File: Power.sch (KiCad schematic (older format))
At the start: 0 parts

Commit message: Added Powercontrol stuff
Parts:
- added C? (x2): C, ~, symbol C
- added F? (x4): FUSE, ~, symbol FUSE
- added L? (x2): INDUCTOR, ~, symbol INDUCTOR
- added P?: CONN_12X2, symbol CONN_12X2
- added R?: R, ~, symbol R
- added SW?: SWITCH_INV, ~, symbol SWITCH_INV
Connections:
- net labels added: +12P, +12V, +3,3V, +5V, -12P, -12V, GND
- wire segments 0 -> 39

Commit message: Fan/Current Module Refactoring
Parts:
- removed F? (x4): FUSE, ~, symbol FUSE
- added TH? (x4): THERMISTOR, ~, symbol THERMISTOR
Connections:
- net labels added: +12C
- wire segments 39 -> 40
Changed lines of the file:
@@
 $Descr A4 11693 8268
 encoding utf-8
-Sheet 5 9
+Sheet 4 9
 Title ""
-Date "6 feb 2014"
+Date "7 feb 2014"
 Rev ""
 Comp ""
@@
 $EndComp
 $Comp
-L FUSE F?
-U 1 1 52F10550
-P 3400 1950
-F 0 "F?" H 3500 2000 40  0000 C CNN
-F 1 "FUSE" H 3300 1900 40  0000 C CNN
-F 2 "~" H 3400 1950 60  0000 C CNN
-F 3 "~" H 3400 1950 60  0000 C CNN
-	1    3400 1950
-	1    0    0    -1
-$EndComp
-$Comp
-L FUSE F?
-U 1 1 52F1055D
-P 3950 2150
-F 0 "F?" H 4050 2200 40  0000 C CNN
-F 1 "FUSE" H 3850 2100 40  0000 C CNN
-F 2 "~" H 3950 2150 60  0000 C CNN
-F 3 "~" H 3950 2150 60  0000 C CNN
-	1    3950 2150
-	1    0    0    -1
-$EndComp
-$Comp
-L FUSE F?
-U 1 1 52F10563
-P 4500 2350
-F 0 "F?" H 4600 2400 40  0000 C CNN
-F 1 "FUSE" H 4400 2300 40  0000 C CNN
-F 2 "~" H 4500 2350 60  0000 C CNN
-F 3 "~" H 4500 2350 60  0000 C CNN
-	1    4500 2350
-	1    0    0    -1
-$EndComp
-$Comp
-L FUSE F?
-U 1 1 52F10569
-P 5050 2550
-F 0 "F?" H 5150 2600 40  0000 C CNN
-F 1 "FUSE" H 4950 2500 40  0000 C CNN
-F 2 "~" H 5050 2550 60  0000 C CNN
-F 3 "~" H 5050 2550 60  0000 C CNN
-	1    5050 2550
-	1    0    0    -1
-$EndComp
-$Comp
 L SWITCH_INV SW?
 U 1 1 52F105A3
@@
 	5400 2550 5300 2550
 Wire Wire Line
-	4300 1500 4300 2150
-Wire Wire Line
-	4300 2150 4200 2150
-Wire Wire Line
-	3750 1500 3750 1950
-Wire Wire Line
-	3750 1950 3650 1950
+	4300 2150 4300 1500
+Wire Wire Line
+	4150 2150 4300 2150
+Wire Wire Line
+	3750 1950 3750 1500
+Wire Wire Line
+	3600 1950 3750 1950
 $Comp
 L INDUCTOR L?
@@
 	8650 2750 8650 2500
 Connection ~ 7800 2750
+$Comp
+L +12C #PWR?
+U 1 1 52F3B02A
+P 3050 1500
+F 0 "#PWR?" H 3050 1470 30  0001 C CNN
+F 1 "+12C" H 3050 1610 40  0000 C CNN
+F 2 "" H 3050 1500 60  0000 C CNN
+F 3 "" H 3050 1500 60  0000 C CNN
+	1    3050 1500
+	1    0    0    -1
+$EndComp
+Wire Wire Line
+	3050 1500 3050 2350
+Connection ~ 3050 2350
+$Comp
+L THERMISTOR TH?
+U 1 1 52F3B361
+P 3350 1950
+F 0 "TH?" V 3450 2000 50  0000 C CNN
+F 1 "THERMISTOR" V 3250 1950 50  0000 C CNN
+F 2 "~" H 3350 1950 60  0000 C CNN
+F 3 "~" H 3350 1950 60  0000 C CNN
+	1    3350 1950
+	0    -1   -1   0
+$EndComp
+$Comp
+L THERMISTOR TH?
+U 1 1 52F3B37D
+P 3900 2150
+F 0 "TH?" V 4000 2200 50  0000 C CNN
+F 1 "THERMISTOR" V 3800 2150 50  0000 C CNN
+F 2 "~" H 3900 2150 60  0000 C CNN
+F 3 "~" H 3900 2150 60  0000 C CNN
+	1    3900 2150
+	0    -1   -1   0
+$EndComp
+$Comp
+L THERMISTOR TH?
+U 1 1 52F3B383
+P 4500 2350
+F 0 "TH?" V 4600 2400 50  0000 C CNN
+F 1 "THERMISTOR" V 4400 2350 50  0000 C CNN
+F 2 "~" H 4500 2350 60  0000 C CNN
+F 3 "~" H 4500 2350 60  0000 C CNN
+	1    4500 2350
+	0    -1   -1   0
+$EndComp
+$Comp
+L THERMISTOR TH?
+U 1 1 52F3B389
+P 5050 2550
+F 0 "TH?" V 5150 2600 50  0000 C CNN
+F 1 "THERMISTOR" V 4950 2550 50  0000 C CNN
+F 2 "~" H 5050 2550 60  0000 C CNN
+F 3 "~" H 5050 2550 60  0000 C CNN
+	1    5050 2550
+	0    -1   -1   0
+$EndComp
 $EndSCHEMATC

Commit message: Am Ende der 4. Woche
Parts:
- added C?: C, ~, symbol C
- added L?: INDUCTOR, ~, symbol INDUCTOR
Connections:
- net labels added: +3.3VP, +5P
- wire segments 40 -> 46
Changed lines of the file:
@@
 Sheet 4 9
 Title ""
-Date "7 feb 2014"
+Date "14 feb 2014"
 Rev ""
 Comp ""
@@
 $EndComp
 $Comp
-L +3,3V #PWR?
-U 1 1 52F10507
-P 3750 1500
-F 0 "#PWR?" H 3750 1460 30  0001 C CNN
-F 1 "+3,3V" H 3750 1610 30  0000 C CNN
-F 2 "" H 3750 1500 60  0000 C CNN
-F 3 "" H 3750 1500 60  0000 C CNN
-	1    3750 1500
-	1    0    0    -1
-$EndComp
-$Comp
 L SWITCH_INV SW?
 U 1 1 52F105A3
@@
 F 3 "" H 4850 1500 60  0000 C CNN
 	1    4850 1500
-	1    0    0    -1
-$EndComp
-$Comp
-L +5V #PWR?
-U 1 1 52F10C00
-P 4300 1500
-F 0 "#PWR?" H 4300 1590 20  0001 C CNN
-F 1 "+5V" H 4300 1590 30  0000 C CNN
-F 2 "" H 4300 1500 60  0000 C CNN
-F 3 "" H 4300 1500 60  0000 C CNN
-	1    4300 1500
 	1    0    0    -1
 $EndComp
@@
 	0    -1   -1   0
 $EndComp
+$Comp
+L +5P #PWR?
+U 1 1 52FDF0C0
+P 4300 1500
+F 0 "#PWR?" H 4300 1630 20  0001 C CNN
+F 1 "+5P" H 4300 1600 30  0000 C CNN
+F 2 "" H 4300 1500 60  0000 C CNN
+F 3 "" H 4300 1500 60  0000 C CNN
+	1    4300 1500
+	1    0    0    -1
+$EndComp
+$Comp
+L +3.3VP #PWR?
+U 1 1 52FDF0CF
+P 3750 1500
+F 0 "#PWR?" H 3800 1530 20  0001 C CNN
+F 1 "+3.3VP" H 3750 1590 30  0000 C CNN
+F 2 "" H 3750 1500 60  0000 C CNN
+F 3 "" H 3750 1500 60  0000 C CNN
+	1    3750 1500
+	1    0    0    -1
+$EndComp
+$Comp
+L INDUCTOR L?
+U 1 1 52FDF0DC
+P 7000 1200
+F 0 "L?" V 6950 1200 40  0000 C CNN
+F 1 "INDUCTOR" V 7100 1200 40  0000 C CNN
+F 2 "~" H 7000 1200 60  0000 C CNN
+F 3 "~" H 7000 1200 60  0000 C CNN
+	1    7000 1200
+	0    -1   -1   0
+$EndComp
+$Comp
+L C C?
+U 1 1 52FDF0E2
+P 7750 1500
+F 0 "C?" H 7750 1600 40  0000 L CNN
+F 1 "C" H 7756 1415 40  0000 L CNN
+F 2 "~" H 7788 1350 30  0000 C CNN
+F 3 "~" H 7750 1500 60  0000 C CNN
+	1    7750 1500
+	1    0    0    -1
+$EndComp
+Wire Wire Line
+	6350 950  6350 1200
+Wire Wire Line
+	6350 1200 6700 1200
+Wire Wire Line
+	7300 1200 8600 1200
+Wire Wire Line
+	7750 1200 7750 1300
+$Comp
+L GND #PWR?
+U 1 1 52FDF0F9
+P 7750 1900
+F 0 "#PWR?" H 7750 1900 30  0001 C CNN
+F 1 "GND" H 7750 1830 30  0001 C CNN
+F 2 "" H 7750 1900 60  0000 C CNN
+F 3 "" H 7750 1900 60  0000 C CNN
+	1    7750 1900
+	1    0    0    -1
+$EndComp
+Wire Wire Line
+	8600 1200 8600 950
+Connection ~ 7750 1200
+$Comp
+L +5P #PWR?
+U 1 1 52FDF142
+P 6350 950
+F 0 "#PWR?" H 6350 1080 20  0001 C CNN
+F 1 "+5P" H 6350 1050 30  0000 C CNN
+F 2 "" H 6350 950 60  0000 C CNN
+F 3 "" H 6350 950 60  0000 C CNN
+	1    6350 950
+	1    0    0    -1
+$EndComp
+$Comp
+L +5V #PWR?
+U 1 1 52FDF14A
+P 8600 950
+F 0 "#PWR?" H 8600 1040 20  0001 C CNN
+F 1 "+5V" H 8600 1040 30  0000 C CNN
+F 2 "" H 8600 950 60  0000 C CNN
+F 3 "" H 8600 950 60  0000 C CNN
+	1    8600 950
+	1    0    0    -1
+$EndComp
+Wire Wire Line
+	7750 1700 7750 1900
 $EndSCHEMATC

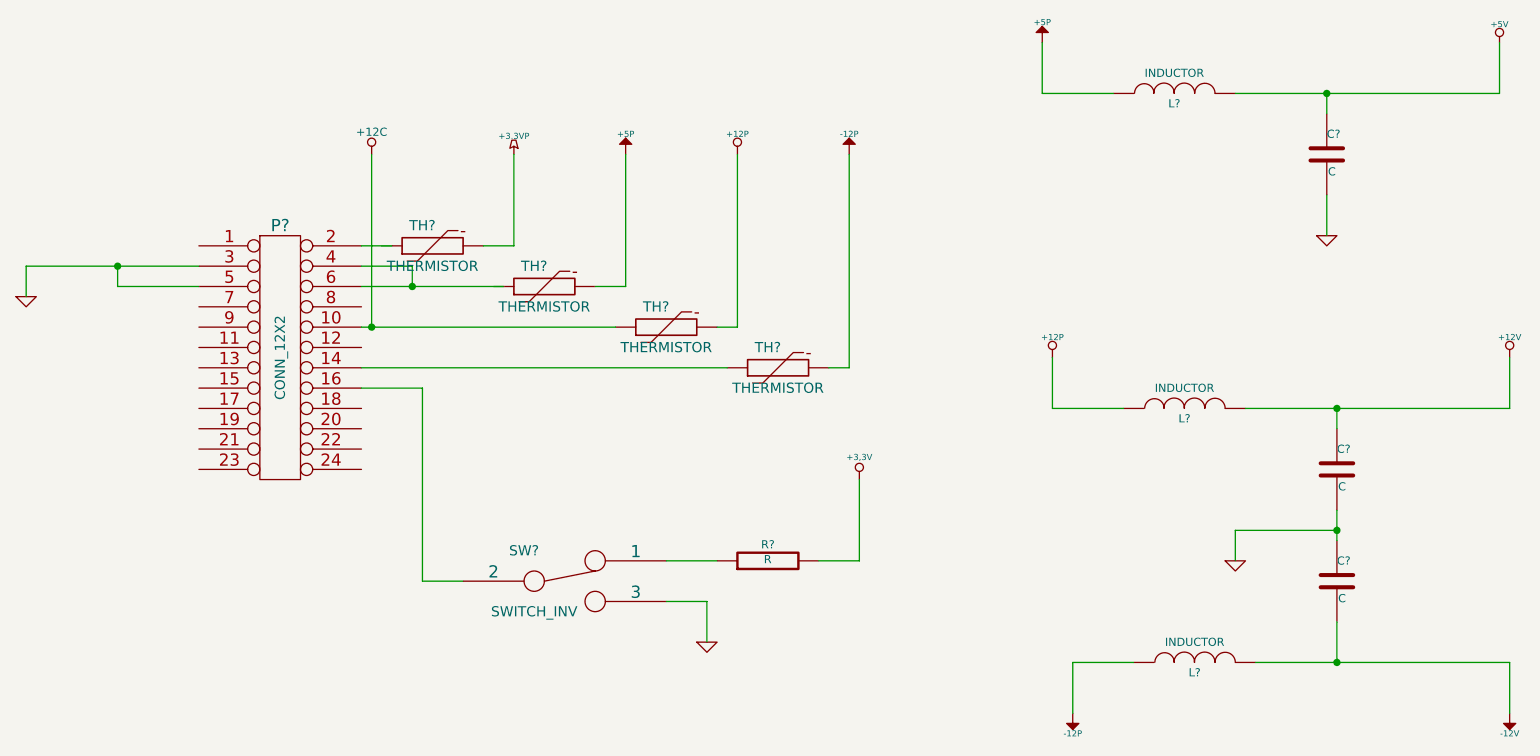
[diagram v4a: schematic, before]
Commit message: Nach Einfuegen Relay-Modul
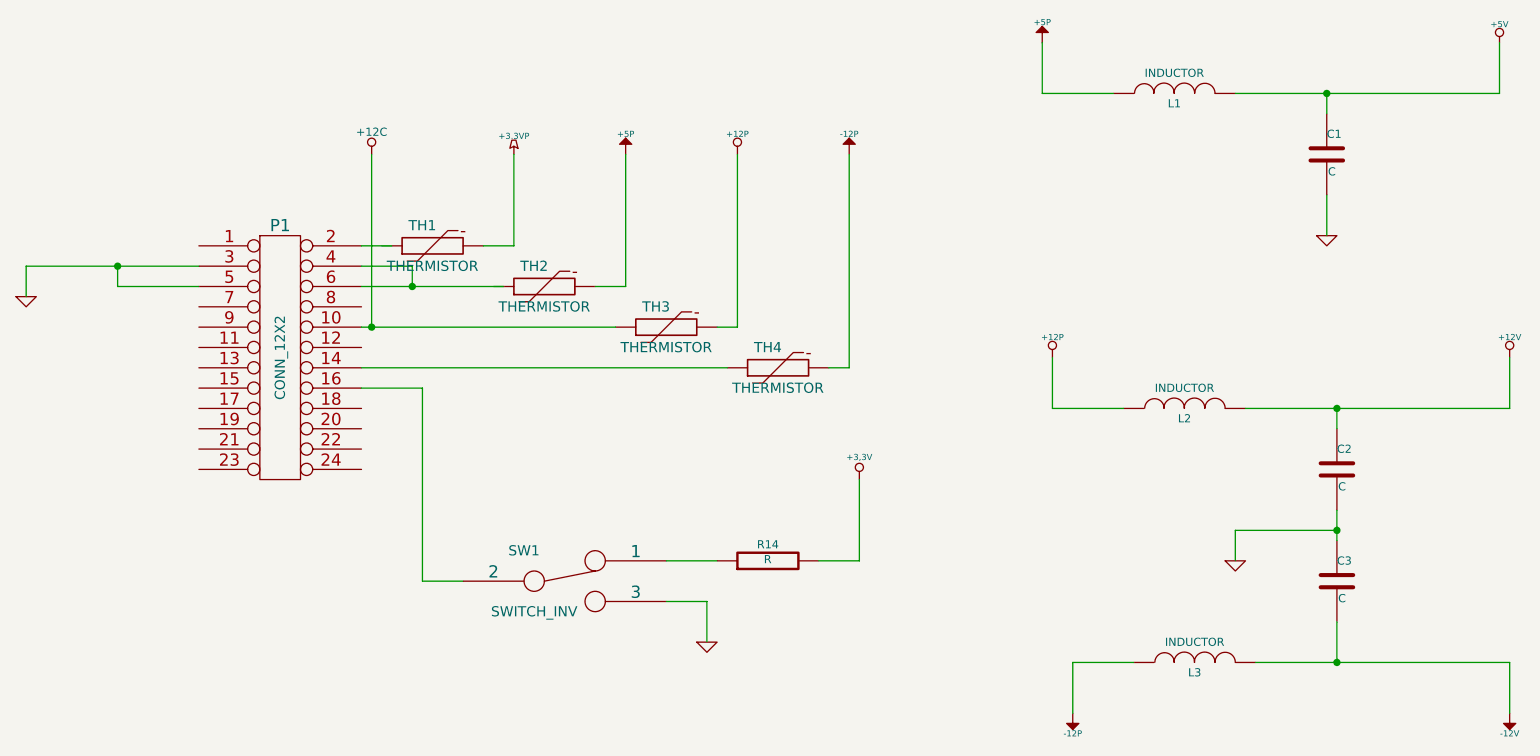
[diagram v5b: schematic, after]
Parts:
- gave numbers to parts that had none: 13
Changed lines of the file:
@@
 Sheet 4 9
 Title ""
-Date "14 feb 2014"
+Date "17 feb 2014"
 Rev ""
 Comp ""
@@
 $EndDescr
 $Comp
-L CONN_12X2 P?
+L CONN_12X2 P1
 U 1 1 52F104E1
 P 2600 2500
-F 0 "P?" H 2600 3150 60  0000 C CNN
+F 0 "P1" H 2600 3150 60  0000 C CNN
 F 1 "CONN_12X2" V 2600 2500 50  0000 C CNN
 F 2 "" H 2600 2500 60  0000 C CNN
@@
 $EndComp
 $Comp
-L GND #PWR?
+L GND #PWR13
 U 1 1 52F104F8
 P 1350 2200
-F 0 "#PWR?" H 1350 2200 30  0001 C CNN
+F 0 "#PWR13" H 1350 2200 30  0001 C CNN
 F 1 "GND" H 1350 2130 30  0001 C CNN
 F 2 "" H 1350 2200 60  0000 C CNN
@@
 $EndComp
 $Comp
-L SWITCH_INV SW?
+L SWITCH_INV SW1
 U 1 1 52F105A3
 P 4000 3600
-F 0 "SW?" H 3800 3750 50  0000 C CNN
+F 0 "SW1" H 3800 3750 50  0000 C CNN
 F 1 "SWITCH_INV" H 3850 3450 50  0000 C CNN
 F 2 "~" H 4000 3600 60  0000 C CNN
@@
 	4700 3700 4700 3900
 $Comp
-L GND #PWR?
+L GND #PWR17
 U 1 1 52F10B9A
 P 4700 3900
-F 0 "#PWR?" H 4700 3900 30  0001 C CNN
+F 0 "#PWR17" H 4700 3900 30  0001 C CNN
 F 1 "GND" H 4700 3830 30  0001 C CNN
 F 2 "" H 4700 3900 60  0000 C CNN
@@
 $EndComp
 $Comp
-L R R?
+L R R14
 U 1 1 52F10BA9
 P 5000 3500
-F 0 "R?" V 5080 3500 40  0000 C CNN
+F 0 "R14" V 5080 3500 40  0000 C CNN
 F 1 "R" V 5007 3501 40  0000 C CNN
 F 2 "~" V 4930 3500 30  0000 C CNN
@@
 	5450 3500 5450 3100
 $Comp
-L +3,3V #PWR?
+L +3,3V #PWR20
 U 1 1 52F10BEB
 P 5450 3100
-F 0 "#PWR?" H 5450 3060 30  0001 C CNN
+F 0 "#PWR20" H 5450 3060 30  0001 C CNN
 F 1 "+3,3V" H 5450 3210 30  0000 C CNN
 F 2 "" H 5450 3100 60  0000 C CNN
@@
 $EndComp
 $Comp
-L +12P #PWR?
+L +12P #PWR18
 U 1 1 52F10BF8
 P 4850 1500
-F 0 "#PWR?" H 4850 1470 30  0001 C CNN
+F 0 "#PWR18" H 4850 1470 30  0001 C CNN
 F 1 "+12P" H 4850 1600 30  0000 C CNN
 F 2 "" H 4850 1500 60  0000 C CNN
@@
 	4850 1500 4850 2350
 $Comp
-L -12P #PWR?
+L -12P #PWR19
 U 1 1 52F10C29
 P 5400 1500
-F 0 "#PWR?" H 5400 1630 20  0001 C CNN
+F 0 "#PWR19" H 5400 1630 20  0001 C CNN
 F 1 "-12P" H 5400 1600 30  0000 C CNN
 F 2 "" H 5400 1500 60  0000 C CNN
@@
 	3600 1950 3750 1950
 $Comp
-L INDUCTOR L?
+L INDUCTOR L2
 U 1 1 52F10CC6
 P 7050 2750
-F 0 "L?" V 7000 2750 40  0000 C CNN
+F 0 "L2" V 7000 2750 40  0000 C CNN
 F 1 "INDUCTOR" V 7150 2750 40  0000 C CNN
 F 2 "~" H 7050 2750 60  0000 C CNN
@@
 $EndComp
 $Comp
-L INDUCTOR L?
+L INDUCTOR L3
 U 1 1 52F10CD3
 P 7100 4000
-F 0 "L?" V 7050 4000 40  0000 C CNN
+F 0 "L3" V 7050 4000 40  0000 C CNN
 F 1 "INDUCTOR" V 7200 4000 40  0000 C CNN
 F 2 "~" H 7100 4000 60  0000 C CNN
@@
 $EndComp
 $Comp
-L C C?
+L C C2
 U 1 1 52F10CDB
 P 7800 3050
-F 0 "C?" H 7800 3150 40  0000 L CNN
+F 0 "C2" H 7800 3150 40  0000 L CNN
 F 1 "C" H 7806 2965 40  0000 L CNN
 F 2 "~" H 7838 2900 30  0000 C CNN
@@
 $EndComp
 $Comp
-L C C?
+L C C3
 U 1 1 52F10CE8
 P 7800 3600
-F 0 "C?" H 7800 3700 40  0000 L CNN
+F 0 "C3" H 7800 3700 40  0000 L CNN
 F 1 "C" H 7806 3515 40  0000 L CNN
 F 2 "~" H 7838 3450 30  0000 C CNN
@@
 $EndComp
 $Comp
-L +12P #PWR?
+L +12P #PWR22
 U 1 1 52F10D27
 P 6400 2500
-F 0 "#PWR?" H 6400 2470 30  0001 C CNN
+F 0 "#PWR22" H 6400 2470 30  0001 C CNN
 F 1 "+12P" H 6400 2600 30  0000 C CNN
 F 2 "" H 6400 2500 60  0000 C CNN
@@
 	6500 4000 6500 4250
 $Comp
-L -12P #PWR?
+L -12P #PWR23
 U 1 1 52F10DDD
 P 6500 4250
-F 0 "#PWR?" H 6500 4380 20  0001 C CNN
+F 0 "#PWR23" H 6500 4380 20  0001 C CNN
 F 1 "-12P" H 6500 4350 30  0000 C CNN
 F 2 "" H 6500 4250 60  0000 C CNN
@@
 $EndComp
 $Comp
-L GND #PWR?
+L GND #PWR24
 U 1 1 52F10DEC
 P 7300 3500
-F 0 "#PWR?" H 7300 3500 30  0001 C CNN
+F 0 "#PWR24" H 7300 3500 30  0001 C CNN
 F 1 "GND" H 7300 3430 30  0001 C CNN
 F 2 "" H 7300 3500 60  0000 C CNN
@@
 Connection ~ 7800 3350
 $Comp
-L -12V #PWR?
+L -12V #PWR28
 U 1 1 52F10E22
 P 8650 4250
-F 0 "#PWR?" H 8650 4380 20  0001 C CNN
+F 0 "#PWR28" H 8650 4380 20  0001 C CNN
 F 1 "-12V" H 8650 4350 30  0000 C CNN
 F 2 "" H 8650 4250 60  0000 C CNN
@@
 Connection ~ 7800 4000
 $Comp
-L +12V #PWR?
+L +12V #PWR27
 U 1 1 52F10E65
 P 8650 2500
-F 0 "#PWR?" H 8650 2450 20  0001 C CNN
+F 0 "#PWR27" H 8650 2450 20  0001 C CNN
 F 1 "+12V" H 8650 2600 30  0000 C CNN
 F 2 "" H 8650 2500 60  0000 C CNN
@@
 Connection ~ 7800 2750
 $Comp
-L +12C #PWR?
+L +12C #PWR14
 U 1 1 52F3B02A
 P 3050 1500
-F 0 "#PWR?" H 3050 1470 30  0001 C CNN
+F 0 "#PWR14" H 3050 1470 30  0001 C CNN
 F 1 "+12C" H 3050 1610 40  0000 C CNN
 F 2 "" H 3050 1500 60  0000 C CNN
@@
 Connection ~ 3050 2350
 $Comp
-L THERMISTOR TH?
+L THERMISTOR TH1
 U 1 1 52F3B361
 P 3350 1950
-F 0 "TH?" V 3450 2000 50  0000 C CNN
+F 0 "TH1" V 3450 2000 50  0000 C CNN
 F 1 "THERMISTOR" V 3250 1950 50  0000 C CNN
 F 2 "~" H 3350 1950 60  0000 C CNN
@@
 $EndComp
 $Comp
-L THERMISTOR TH?
+L THERMISTOR TH2
 U 1 1 52F3B37D
 P 3900 2150
-F 0 "TH?" V 4000 2200 50  0000 C CNN
+F 0 "TH2" V 4000 2200 50  0000 C CNN
 F 1 "THERMISTOR" V 3800 2150 50  0000 C CNN
 F 2 "~" H 3900 2150 60  0000 C CNN
@@
 $EndComp
 $Comp
-L THERMISTOR TH?
+L THERMISTOR TH3
 U 1 1 52F3B383
 P 4500 2350
-F 0 "TH?" V 4600 2400 50  0000 C CNN
+F 0 "TH3" V 4600 2400 50  0000 C CNN
 F 1 "THERMISTOR" V 4400 2350 50  0000 C CNN
 F 2 "~" H 4500 2350 60  0000 C CNN
@@
 $EndComp
 $Comp
-L THERMISTOR TH?
+L THERMISTOR TH4
 U 1 1 52F3B389
 P 5050 2550
-F 0 "TH?" V 5150 2600 50  0000 C CNN
+F 0 "TH4" V 5150 2600 50  0000 C CNN
 F 1 "THERMISTOR" V 4950 2550 50  0000 C CNN
 F 2 "~" H 5050 2550 60  0000 C CNN
@@
 $EndComp
 $Comp
-L +5P #PWR?
+L +5P #PWR16
 U 1 1 52FDF0C0
 P 4300 1500
-F 0 "#PWR?" H 4300 1630 20  0001 C CNN
+F 0 "#PWR16" H 4300 1630 20  0001 C CNN
 F 1 "+5P" H 4300 1600 30  0000 C CNN
 F 2 "" H 4300 1500 60  0000 C CNN
@@
 $EndComp
 $Comp
-L +3.3VP #PWR?
+L +3.3VP #PWR15
 U 1 1 52FDF0CF
 P 3750 1500
-F 0 "#PWR?" H 3800 1530 20  0001 C CNN
+F 0 "#PWR15" H 3800 1530 20  0001 C CNN
 F 1 "+3.3VP" H 3750 1590 30  0000 C CNN
 F 2 "" H 3750 1500 60  0000 C CNN
@@
 $EndComp
 $Comp
-L INDUCTOR L?
+L INDUCTOR L1
 U 1 1 52FDF0DC
 P 7000 1200
-F 0 "L?" V 6950 1200 40  0000 C CNN
+F 0 "L1" V 6950 1200 40  0000 C CNN
 F 1 "INDUCTOR" V 7100 1200 40  0000 C CNN
 F 2 "~" H 7000 1200 60  0000 C CNN
@@
 $EndComp
 $Comp
-L C C?
+L C C1
 U 1 1 52FDF0E2
 P 7750 1500
-F 0 "C?" H 7750 1600 40  0000 L CNN
+F 0 "C1" H 7750 1600 40  0000 L CNN
 F 1 "C" H 7756 1415 40  0000 L CNN
 F 2 "~" H 7788 1350 30  0000 C CNN
@@
 	7750 1200 7750 1300
 $Comp
-L GND #PWR?
+L GND #PWR25
 U 1 1 52FDF0F9
 P 7750 1900
-F 0 "#PWR?" H 7750 1900 30  0001 C CNN
+F 0 "#PWR25" H 7750 1900 30  0001 C CNN
 F 1 "GND" H 7750 1830 30  0001 C CNN
 F 2 "" H 7750 1900 60  0000 C CNN
@@
 Connection ~ 7750 1200
 $Comp
-L +5P #PWR?
+L +5P #PWR21
 U 1 1 52FDF142
 P 6350 950
-F 0 "#PWR?" H 6350 1080 20  0001 C CNN
+F 0 "#PWR21" H 6350 1080 20  0001 C CNN
 F 1 "+5P" H 6350 1050 30  0000 C CNN
 F 2 "" H 6350 950 60  0000 C CNN
@@
 $EndComp
 $Comp
-L +5V #PWR?
+L +5V #PWR26
 U 1 1 52FDF14A
 P 8600 950
-F 0 "#PWR?" H 8600 1040 20  0001 C CNN
+F 0 "#PWR26" H 8600 1040 20  0001 C CNN
 F 1 "+5V" H 8600 1040 30  0000 C CNN
 F 2 "" H 8600 950 60  0000 C CNN
